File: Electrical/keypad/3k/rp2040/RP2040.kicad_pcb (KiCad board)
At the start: 4 copper layers, 66.7 x 67.2 mm, 91 parts, among them J1 Conn_01x04_Socket, J2 Conn_01x04_Socket, P1 USB-TYPE-C-016, Q1 BSS138, Q2 BSS138, SW1 KAN0644-0551B1-A, SW2 KAN0644-0551B1-A, SW3 KAN0644-0551B1-A, SW4 TS-1187A-B-A-B, SW5 TS-1187A-B-A-B, U1 ME6212C33M5G, U2 W25Q16JVSS, U3 PRTR5V0U2X, U4 RP2040, U5 SLSS49E, U6 SLSS49E, U7 SLSS49E, Y1 12MHz

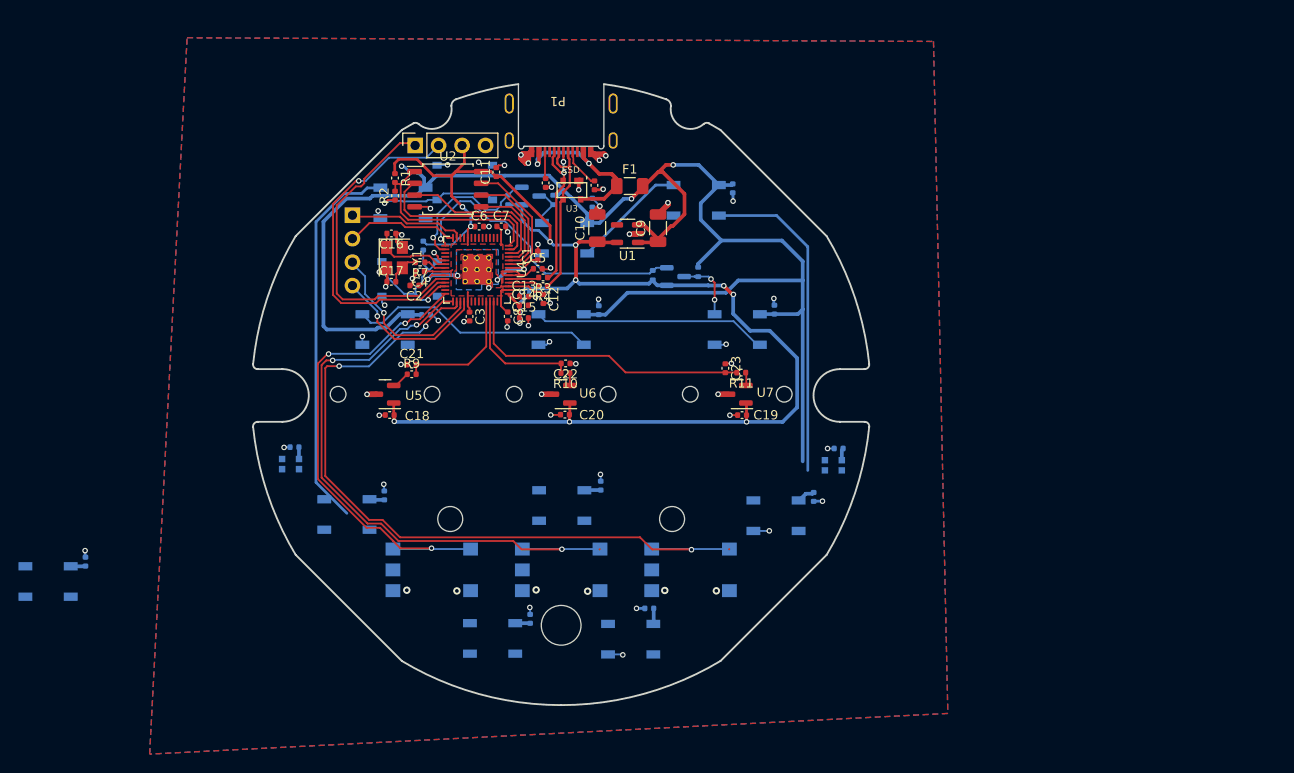
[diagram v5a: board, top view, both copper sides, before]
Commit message: adds instructions to readme, adds the button changes to plate
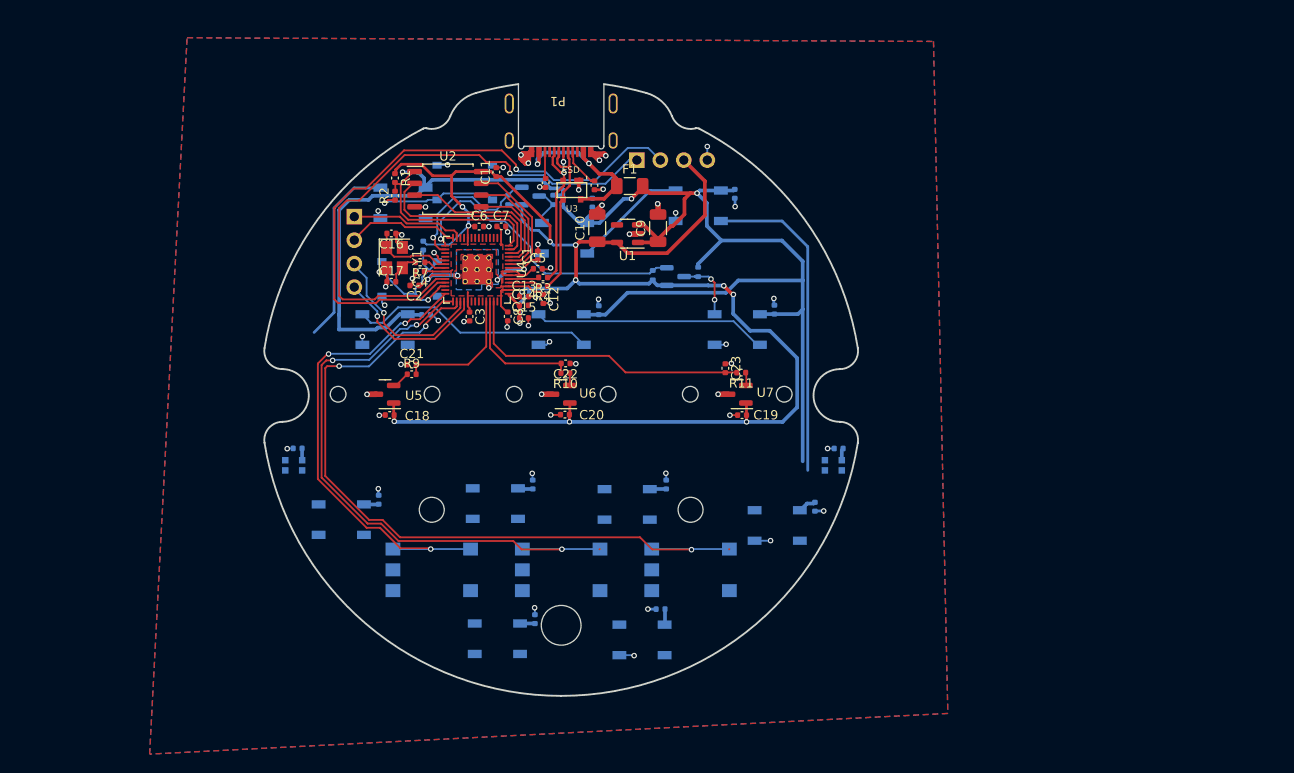
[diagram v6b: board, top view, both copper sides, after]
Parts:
- J2: moved to B.Cu
- moved D9 32.4 mm to (76.2, 113.6)
- moved C29 32.4 mm to (80.3, 111.4)
- moved J2 24.0 mm to (108.2, 74.7), turned to -90 degrees
- moved C31 16.1 mm to (96.9, 109.8)
- moved D8 16.1 mm to (92.9, 111.8)
- moved C32 7.08 mm to (111.4, 109.8)
- moved D6 7.08 mm to (107.1, 111.9)
- moved REF** 2.24 mm to (114.0, 112.5)
- moved REF** 2.24 mm to (86.0, 112.5)
- moved D5 1.23 mm to (108.7, 126.6)
- moved C28 1.23 mm to (110.8, 123.2)
- moved C27 1.07 mm to (127.5, 112.2)
- moved D4 1.07 mm to (123.4, 114.2)
- moved D2 0.63 mm to (114.8, 79.6)
- moved C25 0.63 mm to (118.8, 78.3)
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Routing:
- net SWDIO: track 37.3 -> 64.6 mm
- net SWCLK: track 34.1 -> 59.4 mm, vias 0 -> 1
- net Net-(D10-DO): track 41.2 -> 20.1 mm
- net +3V3: track 178.2 -> 191.6 mm
- net +5V: track 182.0 -> 174.0 mm
- net GND: track 66.7 -> 66.5 mm, vias 65 -> 60
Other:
- board size 66.7 x 67.2 mm -> 64.2 x 66.2 mm

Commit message: misc updates
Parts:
- added ?: , , F.Cu at (126.8, 89.4)
- added REF**: MountingHole_2.7mm_M2.5, MountingHole:MountingHole_2.7mm_M2.5, F.Cu at (126.8, 89.4)
- added REF**: MountingHole_2.7mm_M2.5, MountingHole:MountingHole_2.7mm_M2.5, F.Cu at (115.8, 111.2)
- added REF**: MountingHole_2.7mm_M2.5, MountingHole:MountingHole_2.7mm_M2.5, F.Cu at (84.6, 111.0)
- added REF**: MountingHole_2.7mm_M2.5, MountingHole:MountingHole_2.7mm_M2.5, F.Cu at (72.7, 89.9)
- moved REF** 13.3 mm to (109.5, 100.0)
- moved REF** 13.3 mm to (90.5, 100.0)
- moved C20 2.78 mm to (102.9, 100.9), turned to 180 degrees
- moved C18 2.76 mm to (83.9, 100.9), turned to 180 degrees
- moved C19 2.72 mm to (122.0, 101.0), turned to 180 degrees
- moved C22 1.62 mm to (99.0, 97.2), turned to -90 degrees
- moved D7 1.54 mm to (91.6, 126.4)
- moved C30 1.54 mm to (95.6, 124.3)
- moved C21 1.16 mm to (83.9, 98.0)
- moved R9 1.16 mm to (83.9, 99.0)
- moved C26 0.64 mm to (129.6, 105.4)
- moved D3 0.64 mm to (129.0, 107.2)
- moved C28 0.39 mm to (110.5, 123.0)
- moved D5 0.39 mm to (108.5, 126.3)
- moved C32 0.25 mm to (111.1, 109.7)
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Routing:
- net +5V: track 174.0 -> 169.1 mm
- net +3V3: track 191.6 -> 195.1 mm
- net Net-(D2-DOUT): track 34.8 -> 33.7 mm
- net ADC_IN2: track 14.5 -> 13.9 mm
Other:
- board text added: "SW3"

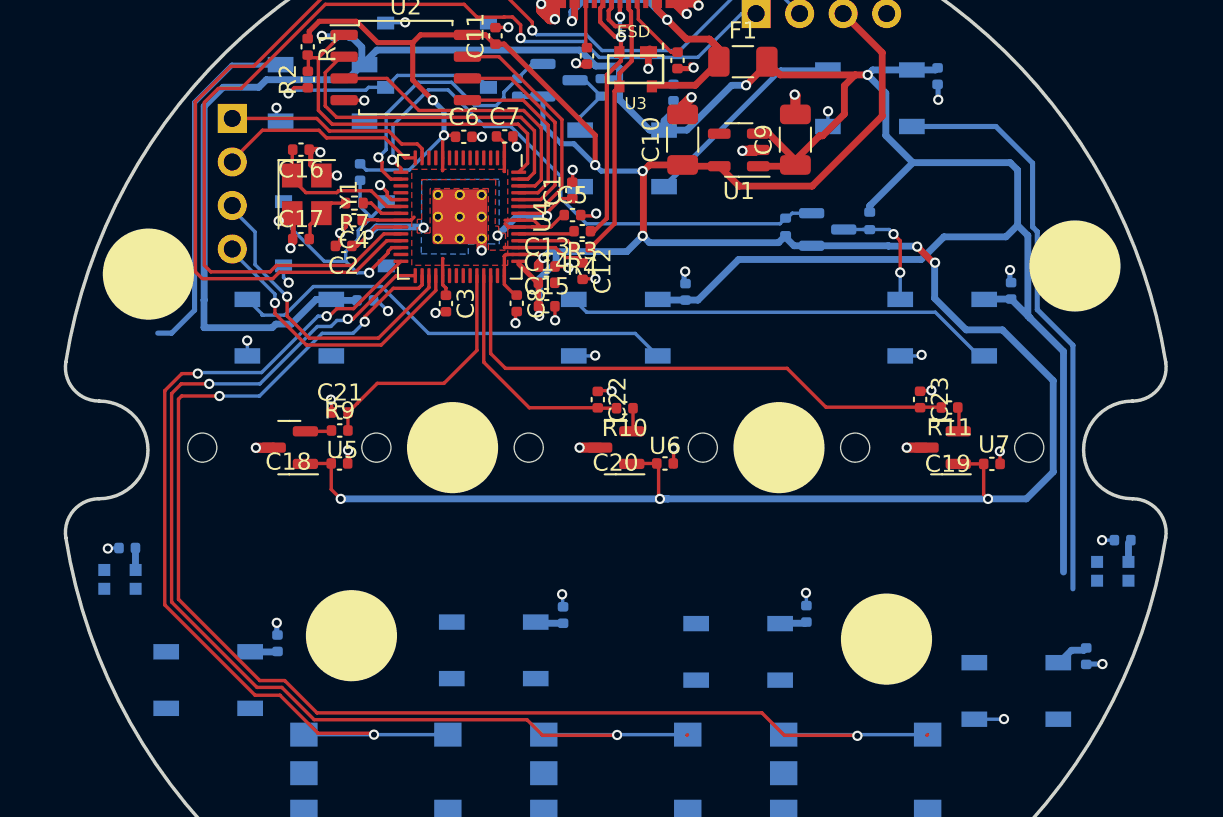
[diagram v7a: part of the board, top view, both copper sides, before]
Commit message: changes led per-key backlights to 2020 and adds more screw holes for tilting issue
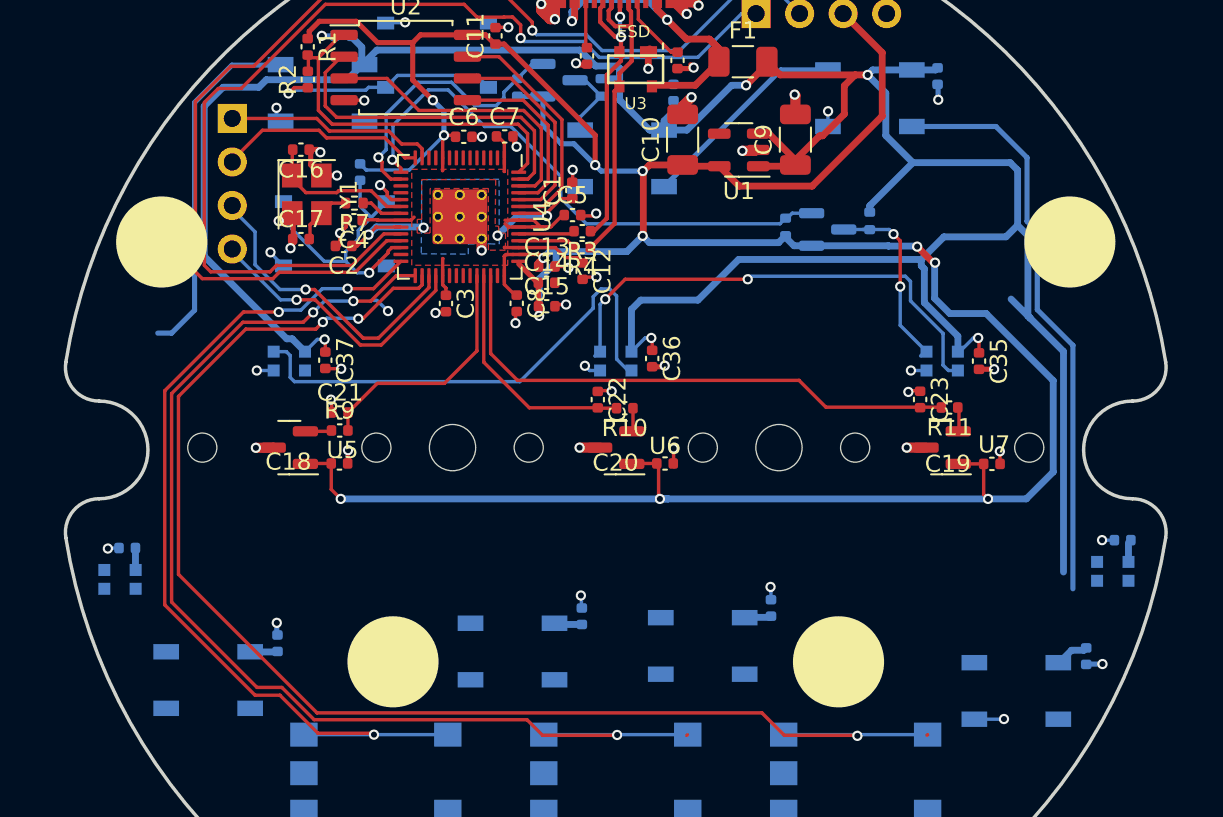
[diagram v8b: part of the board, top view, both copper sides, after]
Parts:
- removed ?: , 
- C35, C36, C37: moved to F.Cu
- D12, D13, D14: value WS2812B -> WS2812-2020; footprint LED_SMD:LED_WS2812B_PLCC4_5.0x5.0mm_P3.2mm -> footprints:LED_WS2812-2020
- moved C35 4.51 mm to (121.2, 95.0), turned to -90 degrees
- moved C36 4.35 mm to (102.1, 94.8), turned to -90 degrees
- moved C37 4.20 mm to (83.0, 94.9), turned to -90 degrees
- moved REF** 3.10 mm to (113.0, 112.5)
- moved REF** 2.86 mm to (87.0, 112.5)
- moved C32 2.10 mm to (109.1, 109.4)
- moved D6 2.10 mm to (105.1, 111.6)
- moved REF** 2.05 mm to (73.5, 88.0)
- moved D12 1.95 mm to (119.0, 95.0), turned to 0 degrees
- moved D13 1.95 mm to (100.0, 95.0), turned to 0 degrees
- moved D14 1.95 mm to (81.0, 95.0), turned to 0 degrees
- moved REF** 1.43 mm to (126.5, 88.0)
- moved C31 1.10 mm to (98.0, 109.8)
- moved D8 1.10 mm to (94.0, 111.9)
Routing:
- net +5V: track 169.1 -> 179.4 mm, vias 2 -> 5
- net Net-(D12-DI): track 7.41 -> 11.2 mm
- net Net-(D12-DO): track 25.3 -> 28.6 mm, vias 0 -> 2
- net Net-(D13-DO): track 26.8 -> 29.1 mm
- net BUTT2: track 80.8 -> 79.9 mm
- net SCL_0: track 17.3 -> 16.6 mm
- net SDA_0: track 18.6 -> 17.9 mm
- net GND: track 66.5 -> 66.7 mm, vias 60 -> 61
